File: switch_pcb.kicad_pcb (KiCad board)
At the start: 2 copper layers, 40 x 34 mm, 6 parts, among them J1 3x5mm, SW1 Microswitch

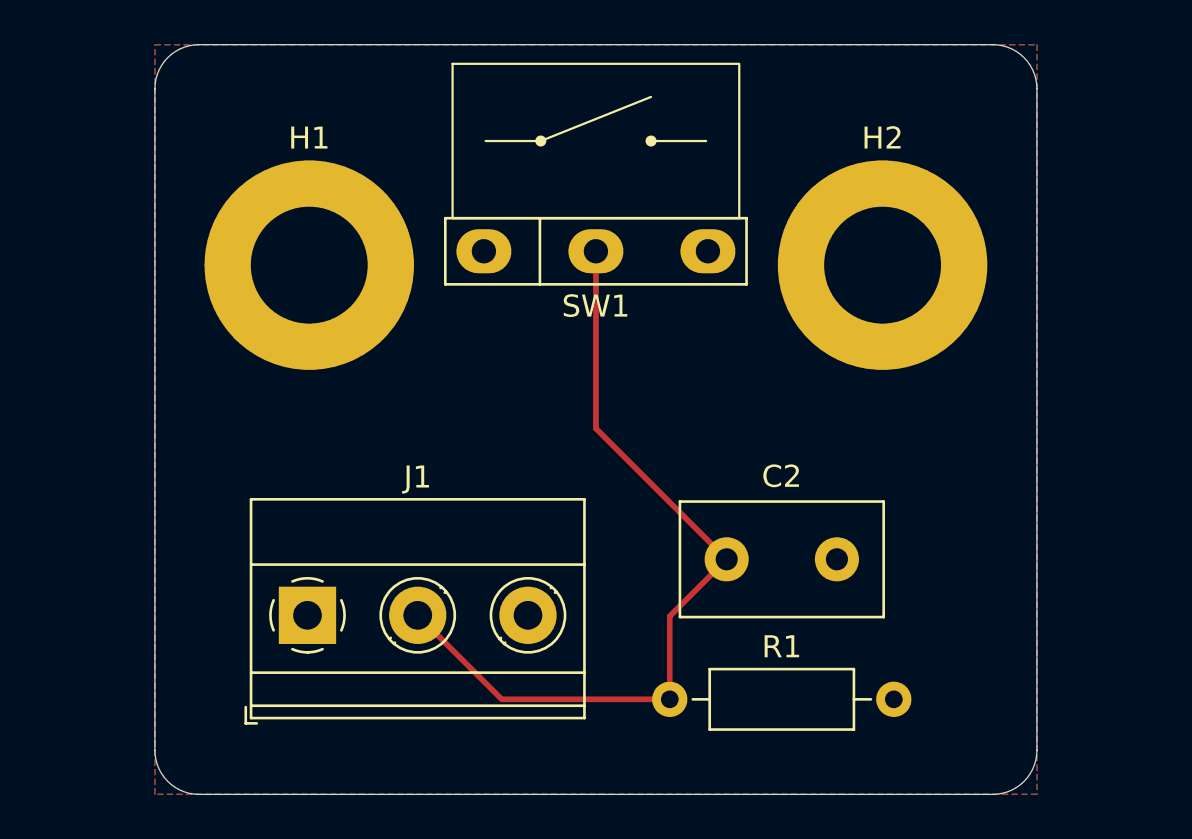
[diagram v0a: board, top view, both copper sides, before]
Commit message: Reworked layout
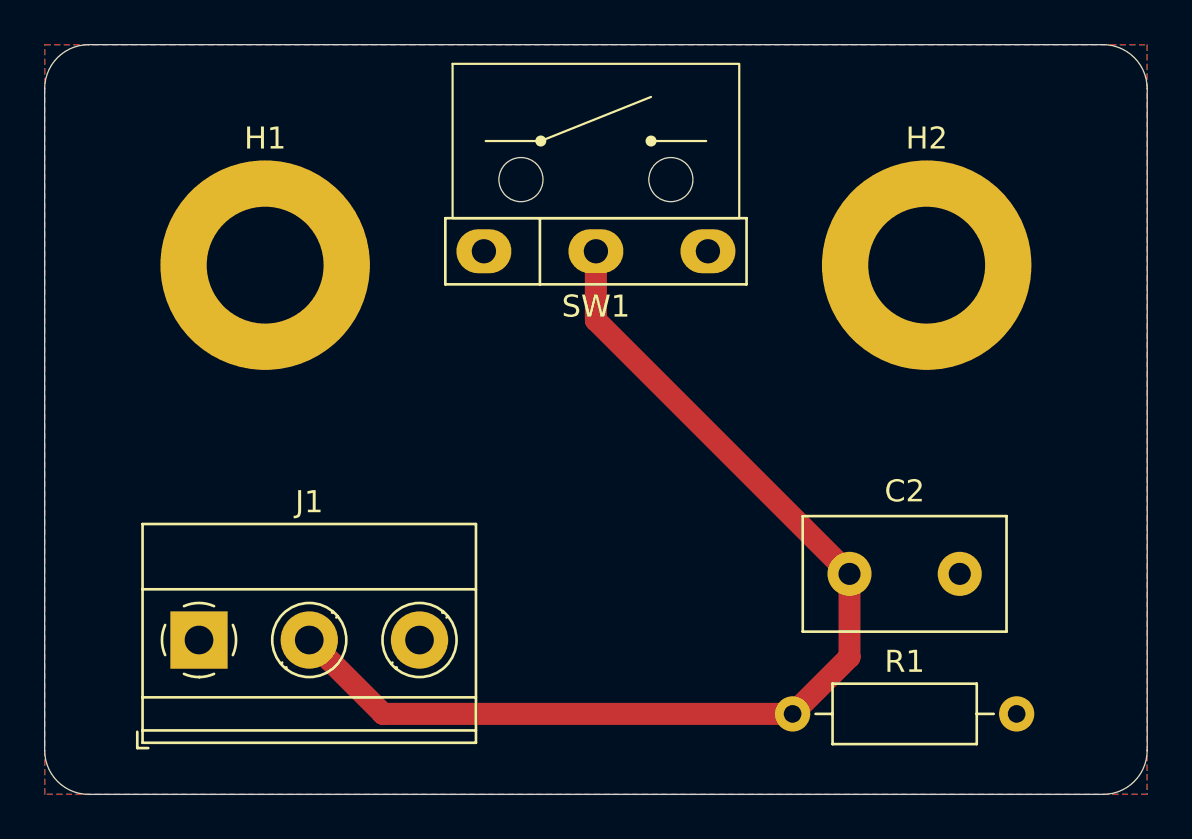
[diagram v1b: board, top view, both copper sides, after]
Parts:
- moved C2 5.61 mm to (141.5, 54.0)
- moved R1 5.61 mm to (138.9, 60.4)
- moved J1 5.05 mm to (112.0, 57.0)
- moved H1 2.00 mm to (115.0, 40.0)
- moved H2 2.00 mm to (145.0, 40.0)
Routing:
- net Net-(J1-Pin_2): track 36.9 -> 50.1 mm
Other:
- board size 40 x 34 mm -> 50 x 34 mm
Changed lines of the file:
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@@
 	(footprint "TerminalBlock_Phoenix:TerminalBlock_Phoenix_MKDS-1,5-3_1x03_P5.00mm_Horizontal"
 		(layer "F.Cu")
-		(at 116.92 55.88)
+		(at 112 57)
 		(descr "Terminal Block Phoenix MKDS-1,5-3, 3 pins, pitch 5mm, size 15x9.8mm^2, drill diamater 1.3mm, pad diameter 2.6mm, see http://www.farnell.com/datasheets/100425.pdf, script-generated using https://github.com/pointhi/kicad-footprint-generator/scripts/TerminalBlock_Phoenix")
 		(tags "THT Terminal Block Phoenix MKDS-1,5-3 pitch 5mm size 15x9.8mm^2 drill 1.3mm pad 2.6mm")
@@
 	(footprint "MountingHole:MountingHole_5.3mm_M5_ISO7380_Pad"
 		(layer "F.Cu")
-		(at 143 40)
+		(at 145 40)
 		(descr "Mounting Hole 5.3mm, M5, ISO7380")
 		(tags "mounting hole 5.3mm m5 iso7380")
@@
 	(footprint "Capacitor_THT:C_Disc_D9.0mm_W5.0mm_P5.00mm"
 		(layer "F.Cu")
-		(at 135.93 53.34)
+		(at 141.5 54)
 		(descr "C, Disc series, Radial, pin pitch=5.00mm, , diameter*width=9*5.0mm^2, Capacitor, http://www.vishay.com/docs/28535/vy2series.pdf")
 		(tags "C Disc series Radial pin pitch 5.00mm  diameter 9mm width 5.0mm Capacitor")
@@
 			(fill none)
 			(layer "F.Fab")
+		)
+		(pad "" np_thru_hole circle
+			(at -3.4 -3.25)
+			(size 2 2)
+			(drill 2)
+			(layers "F&B.Cu" "*.Mask")
+		)
+		(pad "" np_thru_hole circle
+			(at 3.4 -3.25)
+			(size 2 2)
+			(drill 2)
+			(layers "F&B.Cu" "*.Mask")
 		)
 		(pad "1" thru_hole oval
@@
 	(footprint "MountingHole:MountingHole_5.3mm_M5_ISO7380_Pad"
 		(layer "F.Cu")
-		(at 117 40)
+		(at 115 40)
 		(descr "Mounting Hole 5.3mm, M5, ISO7380")
 		(tags "mounting hole 5.3mm m5 iso7380")
@@
 	(footprint "Resistor_THT:R_Axial_DIN0207_L6.3mm_D2.5mm_P10.16mm_Horizontal"
 		(layer "F.Cu")
-		(at 133.35 59.69)
+		(at 138.92 60.35)
 		(descr "Resistor, Axial_DIN0207 series, Axial, Horizontal, pin pitch=10.16mm, 0.25W = 1/4W, length*diameter=6.3*2.5mm^2, http://cdn-reichelt.de/documents/datenblatt/B400/1_4W%23YAG.pdf")
 		(tags "Resistor Axial_DIN0207 series Axial Horizontal pin pitch 10.16mm 0.25W = 1/4W length 6.3mm diameter 2.5mm")
@@
 	)
 	(gr_line
+		(start 152 43)
+		(end 150 50)
+		(stroke
+			(width 0.15)
+			(type default)
+		)
+		(layer "B.SilkS")
+	)
+	(gr_line
 		(start 114 50)
 		(end 116 43)
@@
 	)
 	(gr_rect
-		(start 110 43)
-		(end 150 50)
+		(start 105 43)
+		(end 155 50)
 		(stroke
 			(width 0.1)
@@
 		(layer "B.SilkS")
 	)
+	(gr_line
+		(start 108 50)
+		(end 110 43)
+		(stroke
+			(width 0.15)
+			(type default)
+		)
+		(layer "B.SilkS")
+	)
 	(gr_rect
-		(start 110 30)
-		(end 150 37)
+		(start 105 30)
+		(end 155 37)
 		(stroke
 			(width 0.1)
@@
 	)
 	(gr_line
+		(start 108 37)
+		(end 110 30)
+		(stroke
+			(width 0.15)
+			(type default)
+		)
+		(layer "B.SilkS")
+	)
+	(gr_line
 		(start 130 37)
 		(end 132 30)
@@
 	)
 	(gr_line
+		(start 106 37)
+		(end 108 30)
+		(stroke
+			(width 0.15)
+			(type default)
+		)
+		(layer "B.SilkS")
+	)
+	(gr_line
 		(start 136 37)
 		(end 138 30)
@@
 	)
 	(gr_line
+		(start 152 30)
+		(end 150 37)
+		(stroke
+			(width 0.15)
+			(type default)
+		)
+		(layer "B.SilkS")
+	)
+	(gr_line
 		(start 122 37)
 		(end 124 30)
@@
 	)
 	(gr_line
+		(start 152 50)
+		(end 154 43)
+		(stroke
+			(width 0.15)
+			(type default)
+		)
+		(layer "B.SilkS")
+	)
+	(gr_line
 		(start 118 37)
 		(end 120 30)
@@
 	)
 	(gr_line
-		(start 114 30)
-		(end 112 30)
-		(stroke
-			(width 0.15)
-			(type default)
-		)
-		(layer "B.SilkS")
-	)
-	(gr_line
 		(start 148 50)
 		(end 150 43)
@@
 		(layer "B.SilkS")
 	)
+	(gr_line
+		(start 152 37)
+		(end 154 30)
+		(stroke
+			(width 0.15)
+			(type default)
+		)
+		(layer "B.SilkS")
+	)
+	(gr_line
+		(start 106 50)
+		(end 108 43)
+		(stroke
+			(width 0.15)
+			(type default)
+		)
+		(layer "B.SilkS")
+	)
 	(gr_arc
-		(start 112 64)
-		(mid 110.585786 63.414214)
-		(end 110 62)
+		(start 107 64)
+		(mid 105.585786 63.414214)
+		(end 105 62)
 		(stroke
 			(width 0.05)
@@
 	)
 	(gr_line
-		(start 150 62)
-		(end 150 32)
+		(start 155 62)
+		(end 155 32)
 		(stroke
 			(width 0.05)
@@
 	)
 	(gr_line
-		(start 110 32)
-		(end 110 62)
+		(start 105 32)
+		(end 105 62)
 		(stroke
 			(width 0.05)
@@
 	)
 	(gr_arc
-		(start 150 62)
-		(mid 149.414214 63.414214)
-		(end 148 64)
+		(start 155 62)
+		(mid 154.414214 63.414214)
+		(end 153 64)
 		(stroke
 			(width 0.05)
@@
 	)
 	(gr_arc
-		(start 110 32)
-		(mid 110.585786 30.585786)
-		(end 112 30)
+		(start 105 32)
+		(mid 105.585786 30.585786)
+		(end 107 30)
 		(stroke
 			(width 0.05)
@@
 	)
 	(gr_arc
-		(start 148 30)
-		(mid 149.414214 30.585786)
-		(end 150 32)
+		(start 153 30)
+		(mid 154.414214 30.585786)
+		(end 155 32)
 		(stroke
 			(width 0.05)
@@
 	)
 	(gr_line
-		(start 112 64)
-		(end 148 64)
+		(start 107 64)
+		(end 153 64)
 		(stroke
 			(width 0.05)
@@
 	)
 	(gr_line
-		(start 148 30)
-		(end 112 30)
+		(start 153 30)
+		(end 107 30)
 		(stroke
 			(width 0.05)
@@
 	)
 	(gr_line
-		(start 109 43)
-		(end 151 43)
+		(start 104 43)
+		(end 156 43)
 		(stroke
 			(width 0.1)
@@
 	)
 	(gr_line
-		(start 109 50)
-		(end 151 50)
+		(start 104 50)
+		(end 156 50)
 		(stroke
 			(width 0.1)
@@
 	)
 	(gr_line
-		(start 109 37)
-		(end 151 37)
+		(start 104 37)
+		(end 156 37)
 		(stroke
 			(width 0.1)
@@
 	)
 	(gr_line
-		(start 109 30)
-		(end 151 30)
+		(start 104 30)
+		(end 156 30)
 		(stroke
 			(width 0.1)
@@
 	)
 	(gr_text "J1"
-		(at 121.92 52.07 -0)
+		(at 117 53.19 -0)
 		(layer "B.SilkS")
 		(effects
@@
 	)
 	(gr_text "C2"
-		(at 138.43 53.34 -0)
+		(at 144 54 -0)
 		(layer "B.SilkS")
 		(effects
@@
 	)
 	(gr_text "R1"
-		(at 138.43 59.69 -0)
+		(at 144 60.35 -0)
 		(layer "B.SilkS")
 		(effects
@@
 		(layer "User.1")
 		(pts
-			(xy 110 30) (xy 110 64)
+			(xy 105 30) (xy 105 64)
 		)
 		(height 4)
 		(gr_text "34.0000 mm"
-			(at 104.85 47 90)
+			(at 99.85 47 90)
 			(layer "User.1")
 			(effects
@@
 		(layer "User.1")
 		(pts
-			(xy 110 30) (xy 150 30)
+			(xy 105 30) (xy 155 30)
 		)
 		(height -5)
-		(gr_text "40.0000 mm"
+		(gr_text "50.0000 mm"
 			(at 130 23.85 0)
 			(layer "User.1")
@@
 	)
 	(segment
-		(start 133.35 59.69)
-		(end 125.73 59.69)
-		(width 0.254)
+		(start 141.5 54)
+		(end 130 42.5)
+		(width 1)
 		(layer "F.Cu")
 		(net 2)
 	)
 	(segment
-		(start 130 39.37)
-		(end 130 47.41)
-		(width 0.254)
+		(start 138.92 60.35)
+		(end 120.35 60.35)
+		(width 1)
 		(layer "F.Cu")
 		(net 2)
 	)
 	(segment
-		(start 125.73 59.69)
-		(end 121.92 55.88)
-		(width 0.254)
+		(start 141.5 57.77)
+		(end 138.92 60.35)
+		(width 1)
 		(layer "F.Cu")
 		(net 2)
 	)
 	(segment
-		(start 130 47.41)
-		(end 135.93 53.34)
-		(width 0.254)
+		(start 120.35 60.35)
+		(end 117 57)
+		(width 1)
 		(layer "F.Cu")
 		(net 2)
 	)
 	(segment
-		(start 135.93 53.34)
-		(end 133.35 55.92)
-		(width 0.254)
+		(start 141.5 54)
+		(end 141.5 57.77)
+		(width 1)
 		(layer "F.Cu")
 		(net 2)
 	)
 	(segment
-		(start 133.35 55.92)
-		(end 133.35 59.69)
-		(width 0.254)
+		(start 130 42.5)
+		(end 130 39.37)
+		(width 1)
 		(layer "F.Cu")
 		(net 2)
@@
 		(polygon
 			(pts
-				(xy 110 30) (xy 150 30) (xy 150 64) (xy 110 64)
+				(xy 105 30) (xy 155 30) (xy 155 64) (xy 105 64)
 			)
 		)
@@
 		(polygon
 			(pts
-				(xy 110 30) (xy 150 30) (xy 150 64) (xy 110 64)
-			)
-		)
+				(xy 105 30) (xy 155 30) (xy 155 64) (xy 105 64)
+			)
+		)

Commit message: Improve silkscreen, add SRO logo
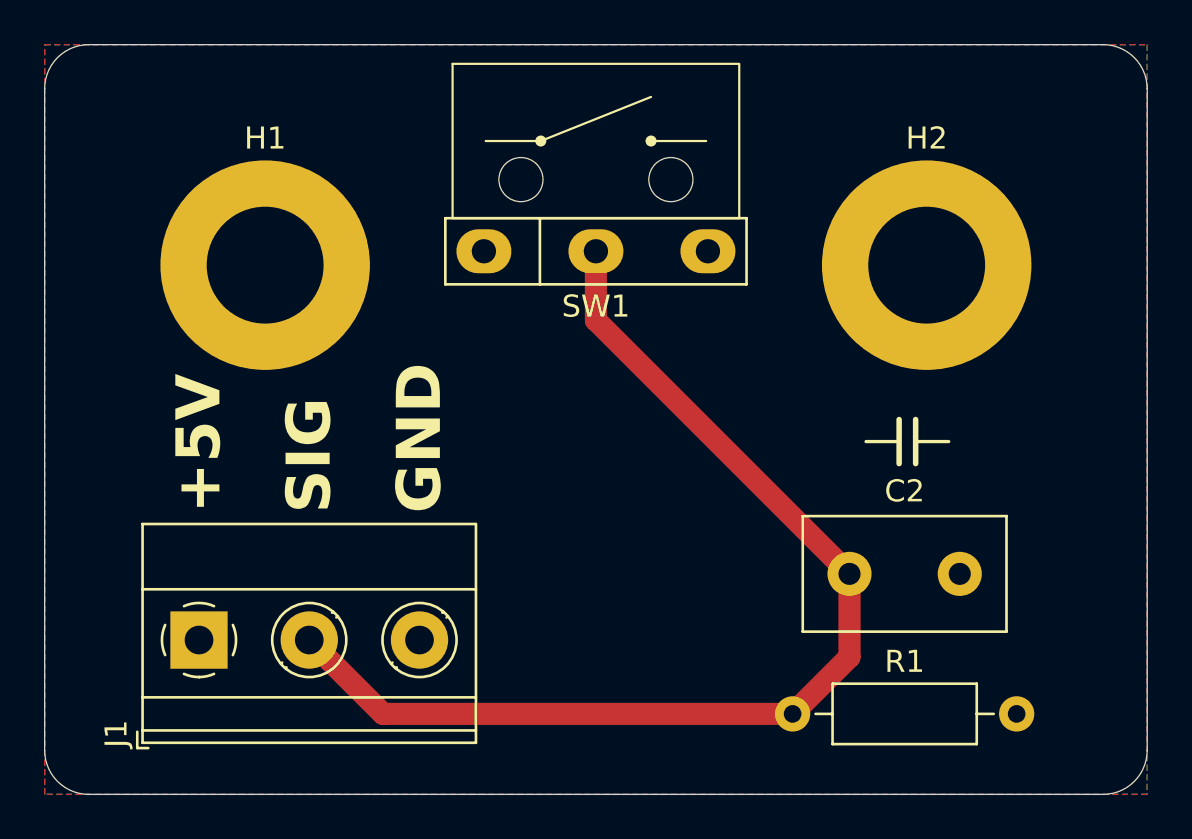
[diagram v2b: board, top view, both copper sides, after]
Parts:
- added G***: LOGO, switch_pcb:SRO-arm-copper, F.Cu at (131.5, 52.8)
- added G***: LOGO, switch_pcb:SRO-arm, B.Cu at (130.2, 54.5)
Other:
- board text added: "+5V"
- board text added: "GND"
- board text added: "JLCJLCJLCJLC"
- board text added: "SIG"
- board text added: "SRO Extrusion Switch Mount WBB 1.0"
